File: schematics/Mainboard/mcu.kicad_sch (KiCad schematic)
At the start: 24 parts, among them J1 Link I2C, J14 Link UART, J3 Mainboard UART, J5 SWD, SW1 BOOT0, SW2 RESET, U1 74HC4051, U2 74HC4051, U3 STM32G0B1CBTx

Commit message: feat(mainboard): Final schematic
Signed-off-by: Andrew Balmos <abalmos@purdue.edu>
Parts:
- added C18: 100n, symbol Device:C_Small
- added D1: Status, symbol Device:LED
- added R7: 270, symbol Device:R_Small_US
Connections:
- net BOOT0/SWCLK: now also C18.1
- net GND: now also C18.2, D1.1 (K)
- net STATUS: now reaches U3.38 (PD0)
- net STATUS: now also R7.1
- new net: D1.2 (A), R7.2
- no-connect marks 16 -> 15
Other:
- moved on the sheet: C1, C17, C19, C2, R1, R2, R3, R4, R5, RN1, RN2, SW1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

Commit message: feat(mainboard): Finished mainboard part selection
Signed-off-by: Andrew Balmos <abalmos@purdue.edu>
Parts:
- C22: renamed from C1; footprint (none) -> Capacitor_SMD:C_0603_1608Metric; LCSC (none) -> C6119867; MPN (none) -> CGA0603X7R104K500JT
- C23: renamed from C2; footprint (none) -> Capacitor_SMD:C_0603_1608Metric; LCSC (none) -> C6119867; MPN (none) -> CGA0603X7R104K500JT
- C24: renamed from C18; footprint (none) -> Capacitor_SMD:C_0603_1608Metric; LCSC (none) -> C6119867; MPN (none) -> CGA0603X7R104K500JT
- C25: renamed from C17; footprint (none) -> Capacitor_SMD:C_0603_1608Metric; LCSC (none) -> C6119867; MPN (none) -> CGA0603X7R104K500JT
- C26: renamed from C19; footprint (none) -> Capacitor_SMD:C_0603_1608Metric; LCSC (none) -> C6119867; MPN (none) -> CGA0603X7R104K500JT
- D1: footprint (none) -> Diode_SMD:D_0603_1608Metric; LCSC (none) -> C2288; MPN (none) -> KT-0603B
- J4: renamed from J1; footprint (none) -> Link_Footprints:TE_3-641215-3; DigiKey (none) -> A30787-ND; LCSC (none) -> C305793; MPN (none) -> 3-641215-3
- J5: renamed from J14; footprint (none) -> Link_Footprints:TE_3-641215-3; DigiKey (none) -> A30787-ND; LCSC (none) -> C305793; MPN (none) -> 3-641215-3
- J6: renamed from J3; footprint (none) -> Link_Footprints:TE_3-641215-3; DigiKey (none) -> A30787-ND; LCSC (none) -> C305793; MPN (none) -> 3-641215-3
- J7: renamed from J5; footprint (none) -> Link_Footprints:TE_3-641215-5; DigiKey (none) -> A30789-ND; LCSC (none) -> C305794; MPN (none) -> 3-641215-5
- JP1, JP2, JP3, JP4: footprint (none) -> Connector_PinHeader_2.54mm:PinHeader_1x03_P2.54mm_Vertical_SMD_Pin1Right; LCSC (none) -> C2883760; MPN (none) -> X6511WVS-03H-C60D48R2
- R2: renamed from R1; footprint (none) -> Resistor_SMD:R_0603_1608Metric; LCSC (none) -> C22369937; MPN (none) -> RCA0310KJLF
- R3: renamed from R2; footprint (none) -> Resistor_SMD:R_0603_1608Metric; LCSC (none) -> C22356630; MPN (none) -> RCA0347KJLF
- R4: renamed from R3; footprint (none) -> Resistor_SMD:R_0603_1608Metric; LCSC (none) -> C22356630; MPN (none) -> RCA0347KJLF
- R5: renamed from R4; footprint (none) -> Resistor_SMD:R_0603_1608Metric; LCSC (none) -> C22369937; MPN (none) -> RCA0310KJLF
- R6: renamed from R7; footprint (none) -> Resistor_SMD:R_0603_1608Metric; LCSC (none) -> C22369858; MPN (none) -> RCA03270RFLF
- R7: renamed from R5; footprint (none) -> Resistor_SMD:R_0603_1608Metric; LCSC (none) -> C22369937; MPN (none) -> RCA0310KJLF
- RN1, RN2: footprint Resistor_THT:R_Array_SIP9 -> Link_Footprints:RESCAXS50P400X160X55-16N; LCSC (none) -> C326649; MPN (none) -> YC248-JR-0710KL
- SW1, SW2: footprint (none) -> Link_Footprints:SW_TS04-66-55-BK-260-SMT; LCSC (none) -> C4364989; MPN (none) -> TS04-66-55-BK-260-SMT
- U1, U2: footprint (none) -> Package_SO:TSSOP-16_4.4x5mm_P0.65mm; LCSC (none) -> C352826; MPN (none) -> CD74HC4051PWR
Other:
- moved on the sheet: C24, C26, R5, R7, SW1, SW2

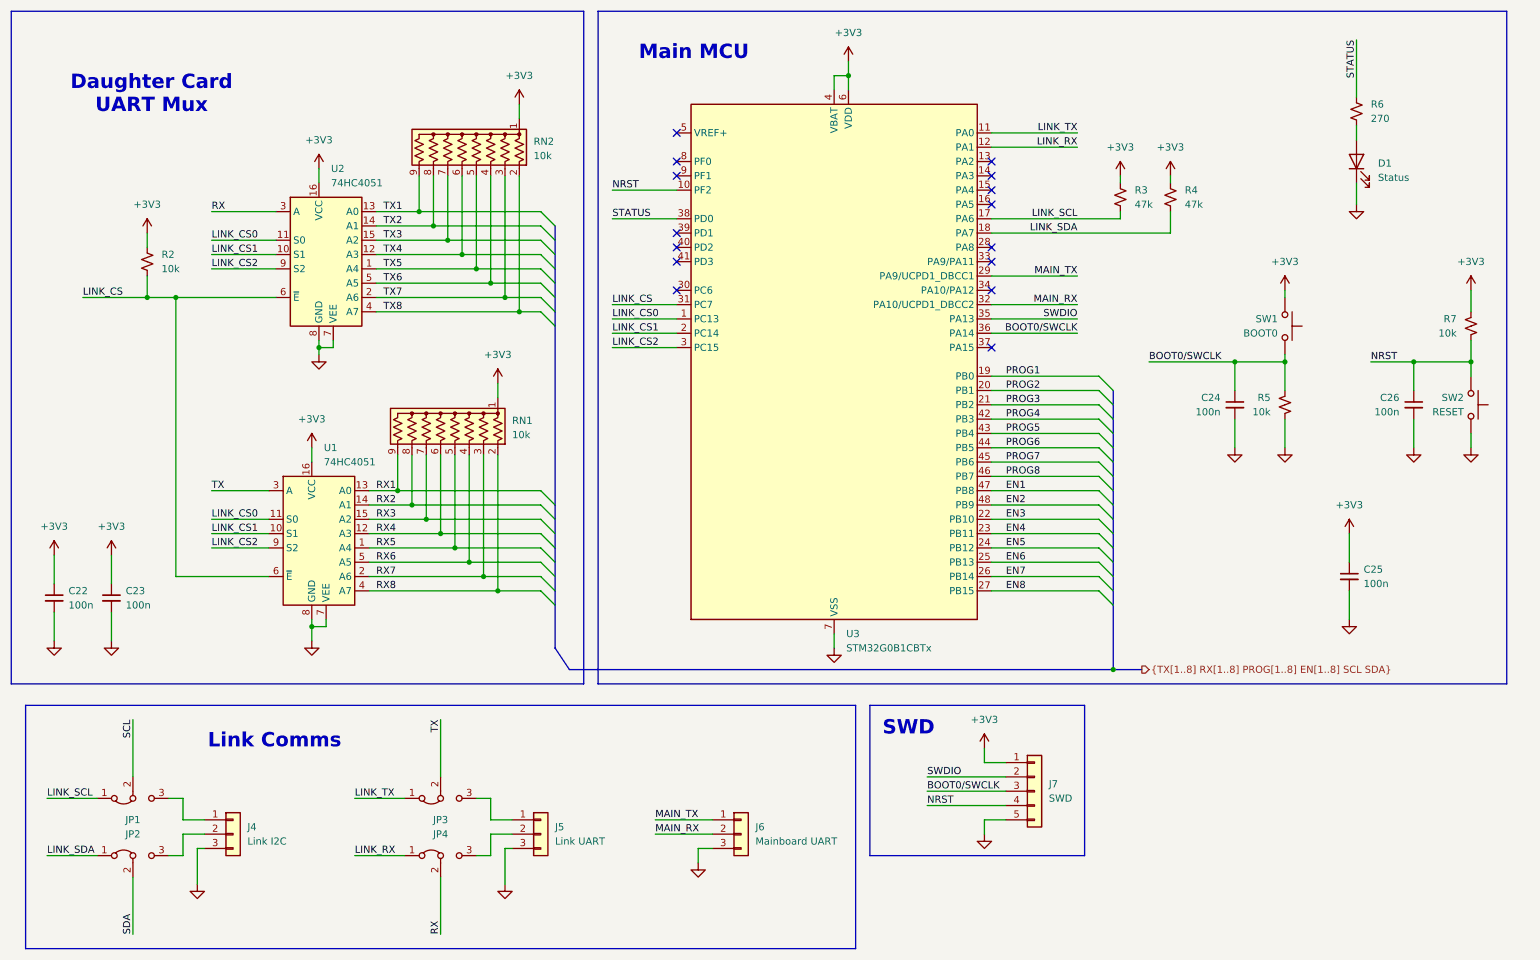
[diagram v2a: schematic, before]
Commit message: release(mainboard): v1.0. Ordered.
Signed-off-by: Andrew Balmos <abalmos@purdue.edu>
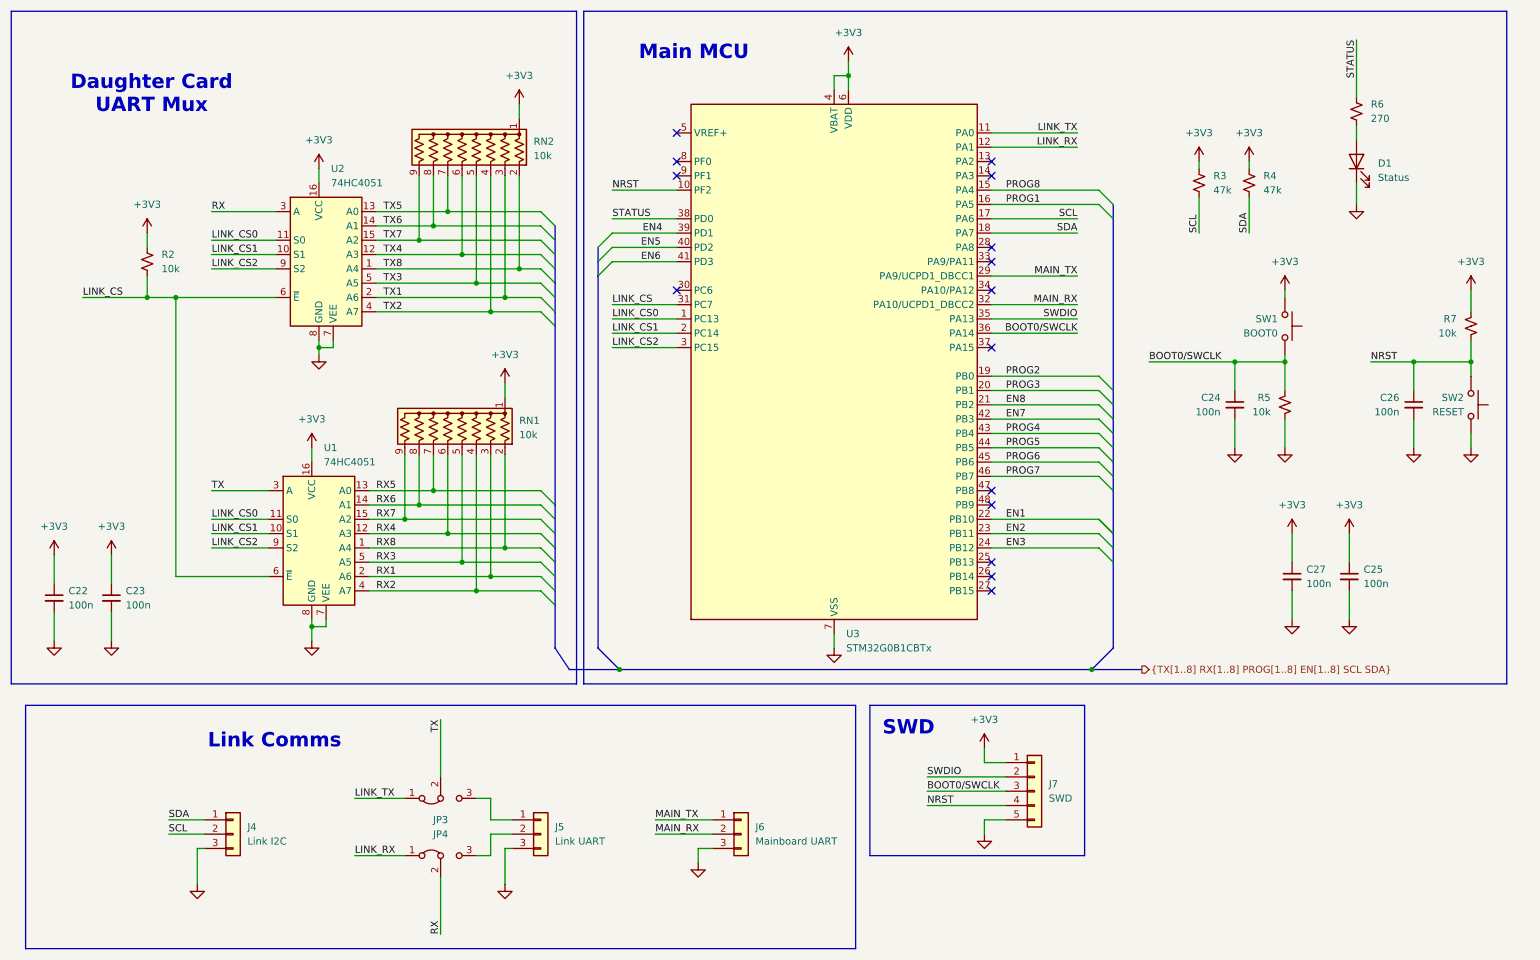
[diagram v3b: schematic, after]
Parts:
- removed JP1, JP2: Jumper_3_Bridged12, Connector_PinHeader_2.54mm:PinHeader_1x03_P2.54mm_Vertical_SMD_Pin1Right, symbol Jumper:Jumper_3_Bridged12
- added C27: 100n, Capacitor_SMD:C_0603_1608Metric, symbol Device:C_Small
- J4, J6: DigiKey A30787-ND -> (none)
- J5: footprint Link_Footprints:TE_3-641215-3 -> Connector_PinHeader_2.54mm:PinHeader_1x03_P2.54mm_Vertical; DigiKey A30787-ND -> (none); LCSC C305793 -> C42431831; MPN 3-641215-3 -> PZ2.54-S03P-A60
- J7: footprint Link_Footprints:TE_3-641215-5 -> Connector_PinHeader_2.54mm:PinHeader_1x05_P2.54mm_Vertical; DigiKey A30789-ND -> (none); FT Rotation Offset (none) -> 90; LCSC C305794 -> C42431825; MPN 3-641215-5 -> PZ2.54-S05P-A60
- JP3, JP4: footprint Connector_PinHeader_2.54mm:PinHeader_1x03_P2.54mm_Vertical_SMD_Pin1Right -> Connector_PinHeader_2.54mm:PinHeader_1x03_P2.54mm_Vertical; LCSC C2883760 -> C42431831; MPN X6511WVS-03H-C60D48R2 -> PZ2.54-S03P-A60; now in the parts list
- RN1, RN2: FT Rotation Offset (none) -> 90
- U3: LCSC (none) -> C2847904; MPN (none) -> STM32G0B1CBT6
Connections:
- net LINK_SCL is gone; now on net SCL: R3.2, U3.17 (PA6)
- net LINK_SDA is gone; now on net SDA: R4.2, U3.18 (PA7)
- net +3V3: now also C27.1
- net EN1: now also U3.22 (PB10); no longer U3.47 (PB8)
- net EN2: now also U3.23 (PB11); no longer U3.48 (PB9)
- net EN3: now also U3.24 (PB12); no longer U3.22 (PB10)
- net EN4: now also U3.39 (PD1); no longer U3.23 (PB11)
- net EN5: now also U3.40 (PD2); no longer U3.24 (PB12)
- net EN6: now also U3.41 (PD3); no longer U3.25 (PB13)
- net EN7: now also U3.42 (PB3); no longer U3.26 (PB14)
- net EN8: now also U3.21 (PB2); no longer U3.27 (PB15)
- net GND: now also C27.2
- net PROG1: now also U3.16 (PA5); no longer U3.19 (PB0)
- net PROG2: now also U3.19 (PB0); no longer U3.20 (PB1)
- net PROG3: now also U3.20 (PB1); no longer U3.21 (PB2)
- net PROG4: now also U3.43 (PB4); no longer U3.42 (PB3)
- net PROG5: now also U3.44 (PB5); no longer U3.43 (PB4)
- net PROG6: now also U3.45 (PB6); no longer U3.44 (PB5)
- net PROG7: now also U3.46 (PB7); no longer U3.45 (PB6)
- net PROG8: now also U3.15 (PA4); no longer U3.46 (PB7)
- net RX1: now also RN1.3 (R2), U1.2 (A6); no longer RN1.9 (R8), U1.13 (A0)
- net RX2: now also RN1.4 (R3), U1.4 (A7); no longer RN1.8 (R7), U1.14 (A1)
- net RX3: now also RN1.5 (R4), U1.5 (A5); no longer RN1.7 (R6), U1.15 (A2)
- net RX5: now also RN1.7 (R6), U1.13 (A0); no longer RN1.5 (R4), U1.1 (A4)
- net RX6: now also RN1.8 (R7), U1.14 (A1); no longer RN1.4 (R3), U1.5 (A5)
- net RX7: now also RN1.9 (R8), U1.15 (A2); no longer RN1.3 (R2), U1.2 (A6)
- net RX8: now also U1.1 (A4); no longer U1.4 (A7)
- net SCL: now also J4.2 (Pin_2)
- net SDA: now also J4.1 (Pin_1)
- net TX1: now also RN2.3 (R2), U2.2 (A6); no longer RN2.9 (R8), U2.13 (A0)
- net TX2: now also RN2.4 (R3), U2.4 (A7); no longer RN2.8 (R7), U2.14 (A1)
- net TX3: now also RN2.5 (R4), U2.5 (A5); no longer RN2.7 (R6), U2.15 (A2)
- net TX5: now also RN2.7 (R6), U2.13 (A0); no longer RN2.5 (R4), U2.1 (A4)
- net TX6: now also RN2.8 (R7), U2.14 (A1); no longer RN2.4 (R3), U2.5 (A5)
- net TX7: now also RN2.9 (R8), U2.15 (A2); no longer RN2.3 (R2), U2.2 (A6)
- net TX8: now also U2.1 (A4); no longer U2.4 (A7)
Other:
- moved on the sheet: R3, R4, RN1
